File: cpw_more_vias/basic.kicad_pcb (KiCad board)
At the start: 2 copper layers, 14 x 60 mm, 3 parts

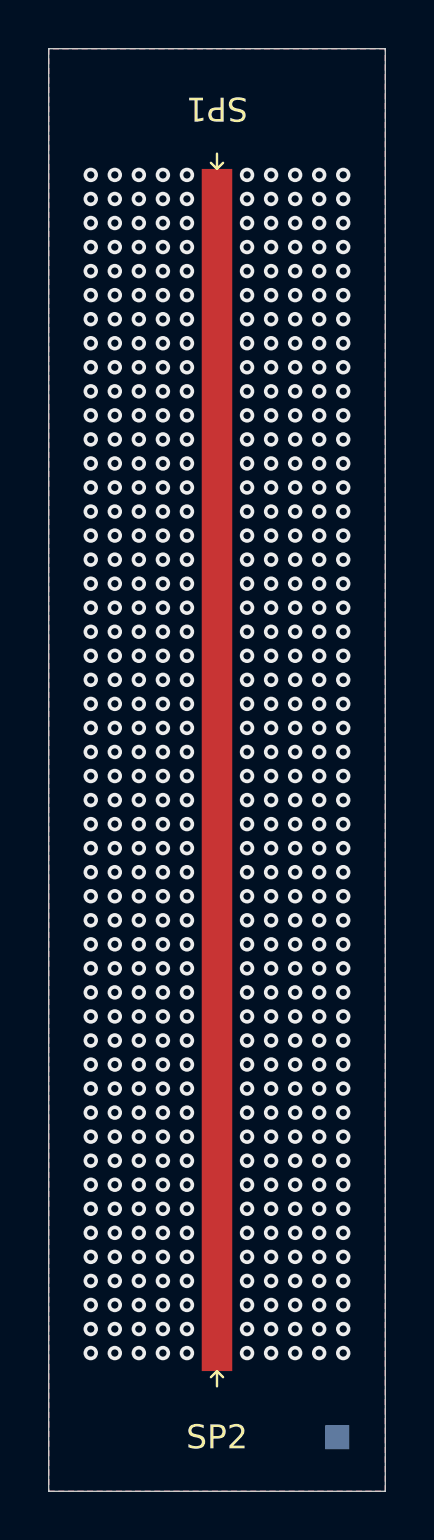
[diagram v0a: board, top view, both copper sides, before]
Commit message: add cpw_fewer_vias
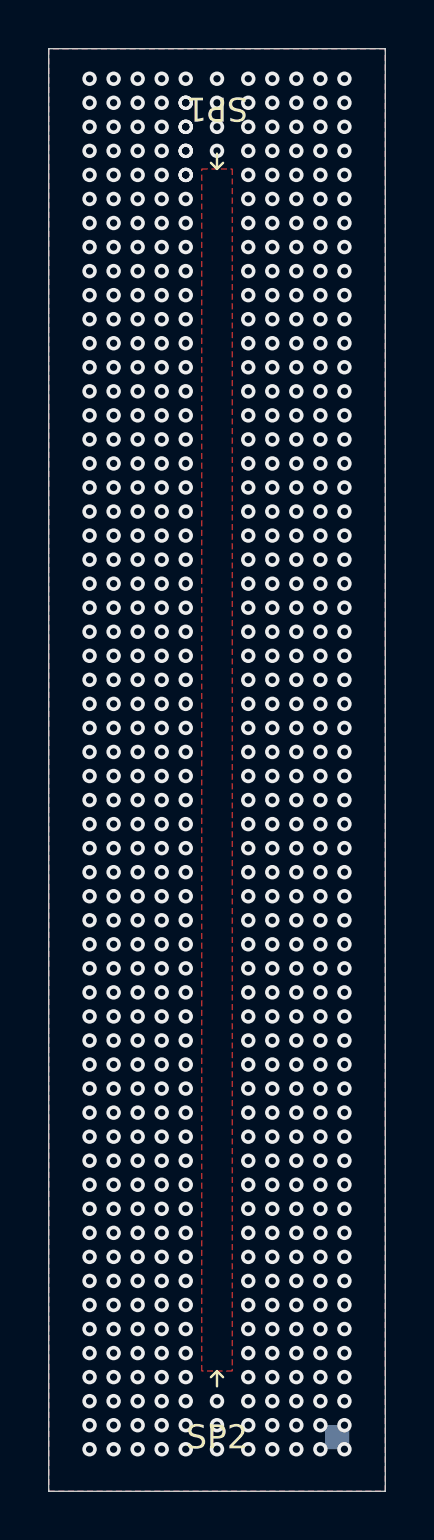
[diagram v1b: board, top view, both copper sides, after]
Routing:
- net GND: vias 500 -> 591
- added copper zone on F.Cu, net (none)
